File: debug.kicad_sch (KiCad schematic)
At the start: 36 parts, among them J701 USB4105-GF-A, J702 Conn_02x10_Odd_Even, U701 USBLC6-2SC6, U702 FT231XQ, U703 TCA9554PW

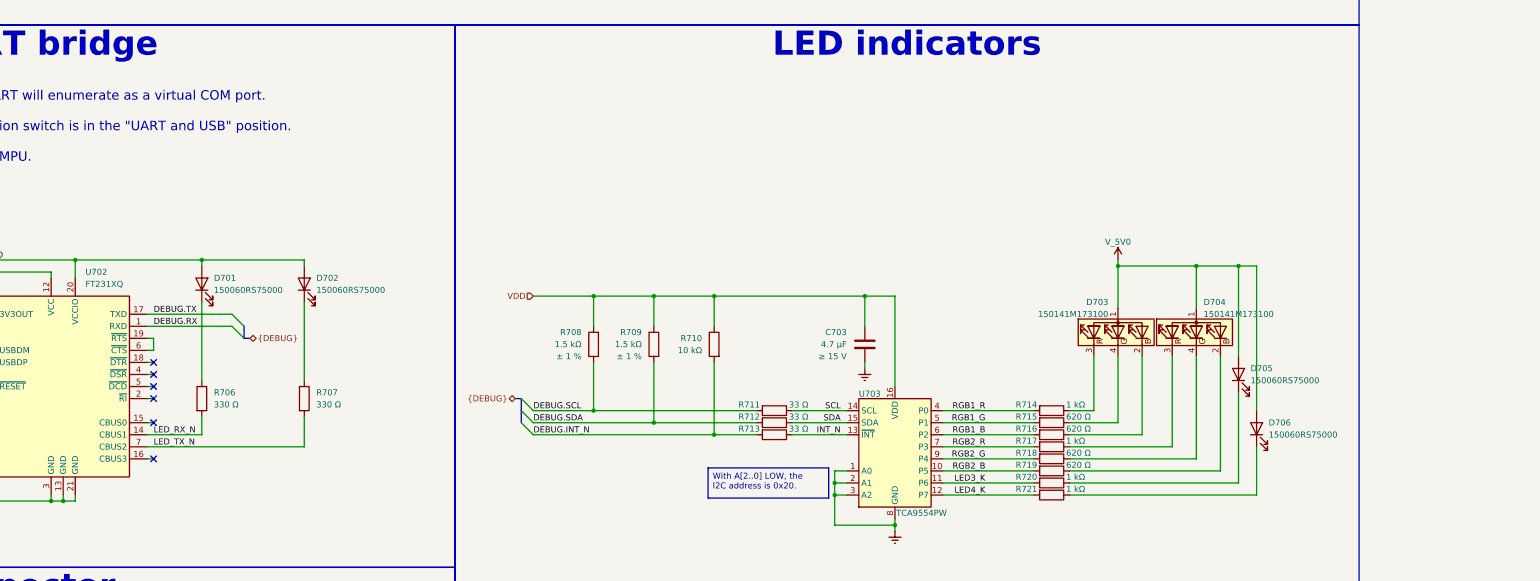
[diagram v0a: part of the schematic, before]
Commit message: Add series termination, assign netclasses, fill schemas' descriptions
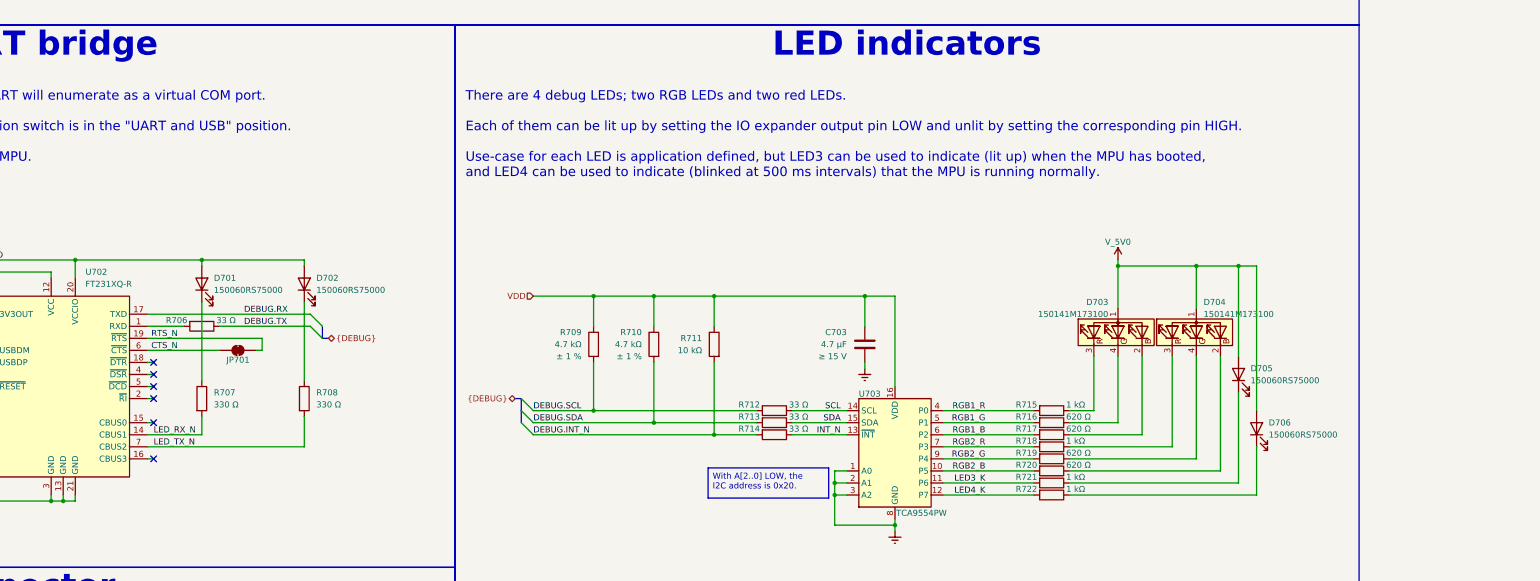
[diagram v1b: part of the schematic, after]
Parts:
- removed R708: 1.5 kΩ, perfect_footprints:R_0402_1005Metric, symbol Device:R
- added JP701: SolderJumper_2_Bridged, Jumper:SolderJumper-2_P1.3mm_Bridged_Pad1.0x1.5mm, symbol Jumper:SolderJumper_2_Bridged
- added R706: 33 Ω, perfect_footprints:R_0402_1005Metric, symbol Device:R
- added R710: 4.7 kΩ, perfect_footprints:R_0402_1005Metric, symbol Device:R
- R709: value 1.5 kΩ -> 4.7 kΩ
- U702: value FT231XQ -> FT231XQ-R; Digi-Key Part Number (none) -> 768-1128-1-ND; MPN (none) -> FT231XQ-R; Manufacturer (none) -> FTDI, Future Technology Devices International Ltd
- renumbered R706 to R707, R707 to R708, R710 to R711, R711 to R712, R712 to R713, R713 to R714, R714 to R715, R715 to R716, R716 to R717, R717 to R718, R718 to R719, R719 to R720, R720 to R721, R721 to R722
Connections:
- net DEBUG.RX: now also U702.17 (TXD); no longer U702.1 (RXD)
- net DEBUG.SCL: now also R709.2
- net DEBUG.SDA: now also R710.2; no longer R709.2
- net DEBUG.TX: now also R706.1; no longer U702.17 (TXD)
- net VDD: now also R710.1
- net CTS_N: now reaches U702.6 (~{CTS})
- net CTS_N: now also JP701.1 (A); no longer U702.19 (~{RTS})
- new net: R706.2, U702.1 (RXD)
- new net RTS_N: JP701.2 (B), U702.19 (~{RTS})

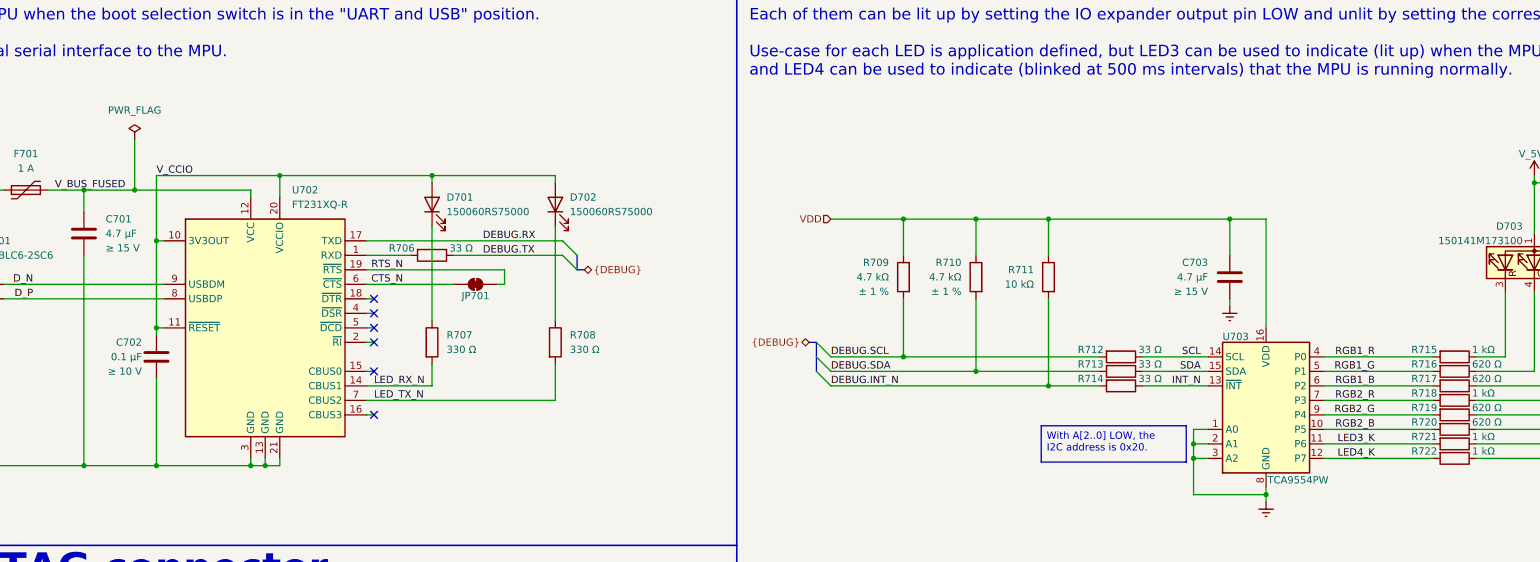
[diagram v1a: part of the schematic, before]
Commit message: Add test points, assign netclasses and clean-up
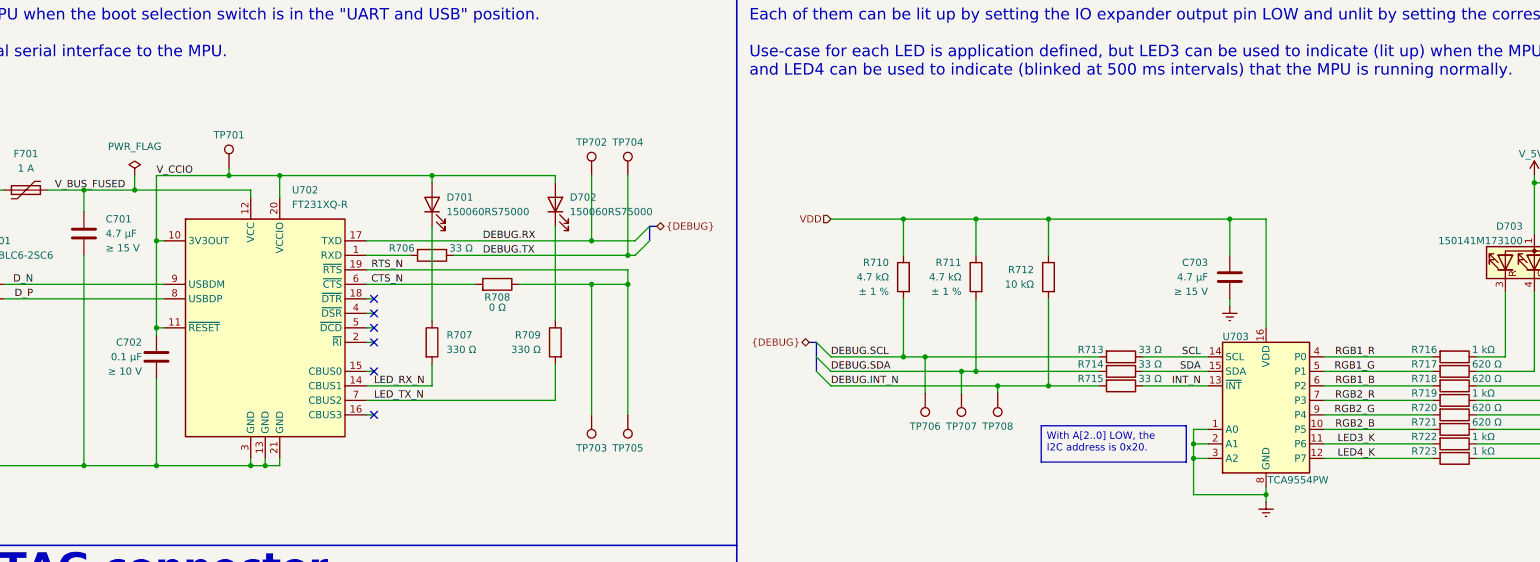
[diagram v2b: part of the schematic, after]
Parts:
- removed JP701: SolderJumper_2_Bridged, Jumper:SolderJumper-2_P1.3mm_Bridged_Pad1.0x1.5mm, symbol Jumper:SolderJumper_2_Bridged
- added R708: 0 Ω, Resistor_SMD:R_0805_2012Metric, symbol Device:R
- added TP701, TP702, TP703, TP704, TP705, TP706, TP707, TP708: TestPoint, TestPoint:TestPoint_Pad_D1.0mm, symbol Connector:TestPoint
- renumbered R708 to R709, R709 to R710, R710 to R711, R711 to R712, R712 to R713, R713 to R714, R714 to R715, R715 to R716, R716 to R717, R717 to R718, R718 to R719, R719 to R720, R720 to R721, R721 to R722, R722 to R723
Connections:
- net CTS_N: now also R708.2
- net DEBUG.INT_N: now also TP708.1
- net DEBUG.RX: now also TP702.1
- net DEBUG.SCL: now also TP706.1
- net DEBUG.SDA: now also TP707.1
- net DEBUG.TX: now also TP704.1
- net RTS_N: now also R708.1, TP703.1, TP705.1
- net V_CCIO: now also TP701.1

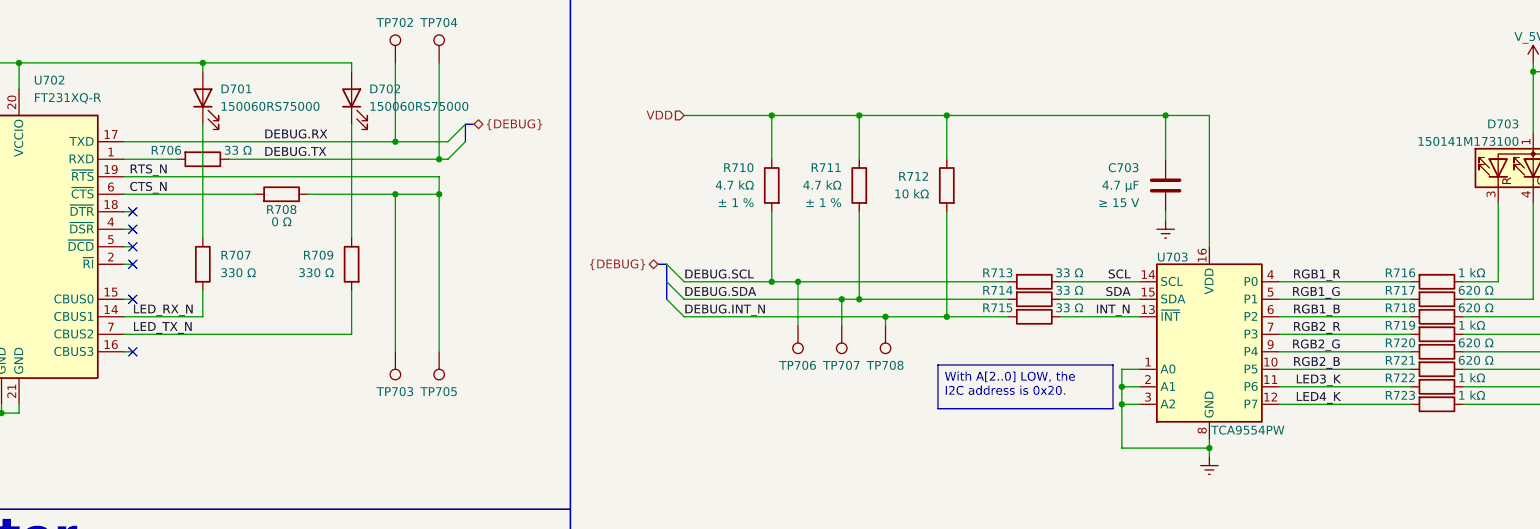
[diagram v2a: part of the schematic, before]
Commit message: Add series termination, refactor schematics
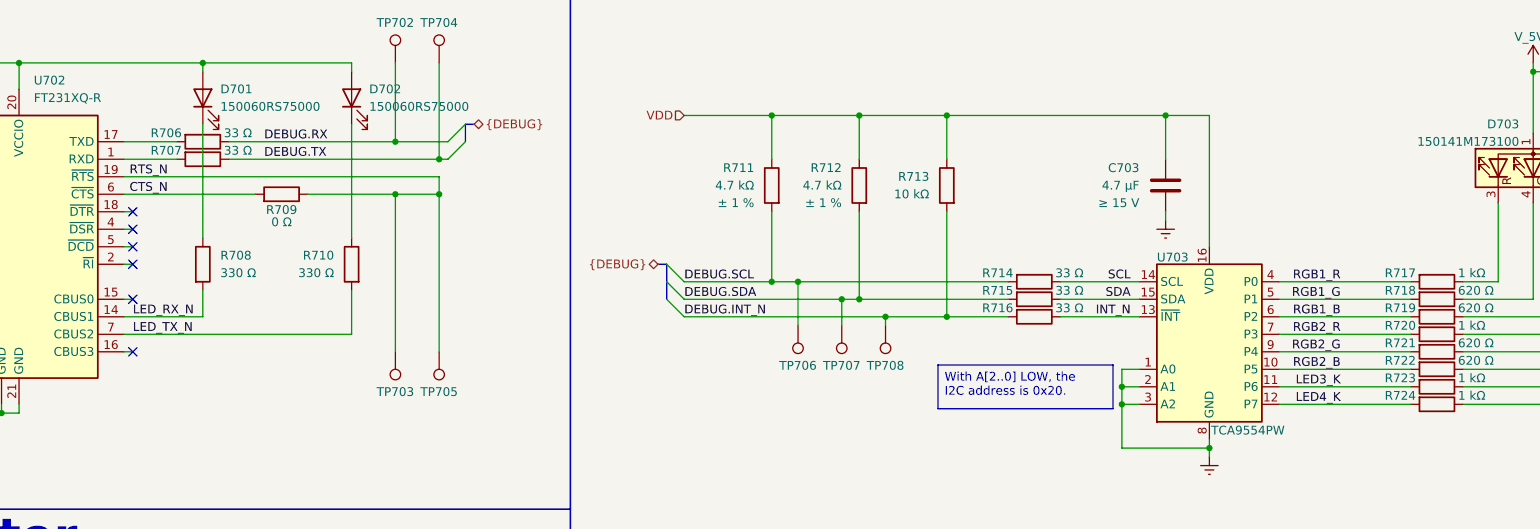
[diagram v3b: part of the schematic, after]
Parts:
- added R706: 33 Ω, perfect_footprints:R_0402_1005Metric, symbol Device:R
- renumbered R706 to R707, R707 to R708, R708 to R709, R709 to R710, R710 to R711, R711 to R712, R712 to R713, R713 to R714, R714 to R715, R715 to R716, R716 to R717, R717 to R718, R718 to R719, R719 to R720, R720 to R721, R721 to R722, R722 to R723, R723 to R724
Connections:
- net DEBUG.RX: now also R706.1; no longer U702.17 (TXD)
- new net: R706.2, U702.17 (TXD)
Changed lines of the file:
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@@
 	(wire
 		(pts
+			(xy 166.37 111.76) (xy 190.5 111.76)
+		)
+		(stroke
+			(width 0)
+			(type default)
+		)
+	)
+	(wire
+		(pts
 			(xy 74.93 200.66) (xy 76.2 200.66)
 		)
@@
 	(wire
 		(pts
-			(xy 151.13 111.76) (xy 190.5 111.76)
+			(xy 151.13 111.76) (xy 158.75 111.76)
 		)
 		(stroke
@@
 		(on_board yes)
 		(dnp no)
-		(property "Reference" "R721"
+		(property "Reference" "R722"
 			(at 338.582 144.272 90)
 			(effects
@@
 			(project "linux-sbc"
 				(path "/fa11a02f-8043-4153-ab69-88d766503017/5e32b227-0684-45b9-8c92-9550e4036164"
-					(reference "R721")
+					(reference "R722")
 					(unit 1)
 				)
@@
 		(on_board yes)
 		(dnp no)
-		(property "Reference" "R715"
+		(property "Reference" "R716"
 			(at 280.162 136.652 90)
 			(effects
@@
 			(project "linux-sbc"
 				(path "/fa11a02f-8043-4153-ab69-88d766503017/5e32b227-0684-45b9-8c92-9550e4036164"
-					(reference "R715")
+					(reference "R716")
 					(unit 1)
 				)
@@
 		(on_board yes)
 		(dnp no)
-		(property "Reference" "R716"
+		(property "Reference" "R717"
 			(at 338.582 131.572 90)
 			(effects
@@
 			(project "linux-sbc"
 				(path "/fa11a02f-8043-4153-ab69-88d766503017/5e32b227-0684-45b9-8c92-9550e4036164"
-					(reference "R716")
+					(reference "R717")
 					(unit 1)
 				)
@@
 		(on_board yes)
 		(dnp no)
-		(property "Reference" "R710"
+		(property "Reference" "R711"
 			(at 242.57 115.57 0)
 			(effects
@@
 			(project "linux-sbc"
 				(path "/fa11a02f-8043-4153-ab69-88d766503017/5e32b227-0684-45b9-8c92-9550e4036164"
-					(reference "R710")
+					(reference "R711")
 					(unit 1)
 				)
@@
 		(on_board yes)
 		(dnp no)
-		(property "Reference" "R720"
+		(property "Reference" "R721"
 			(at 338.582 141.732 90)
 			(effects
@@
 			(project "linux-sbc"
 				(path "/fa11a02f-8043-4153-ab69-88d766503017/5e32b227-0684-45b9-8c92-9550e4036164"
-					(reference "R720")
+					(reference "R721")
 					(unit 1)
 				)
@@
 		(on_board yes)
 		(dnp no)
-		(property "Reference" "R713"
+		(property "Reference" "R714"
 			(at 280.162 131.572 90)
 			(effects
@@
 			(project "linux-sbc"
 				(path "/fa11a02f-8043-4153-ab69-88d766503017/5e32b227-0684-45b9-8c92-9550e4036164"
-					(reference "R713")
+					(reference "R714")
 					(unit 1)
 				)
@@
 		(on_board yes)
 		(dnp no)
-		(property "Reference" "R714"
+		(property "Reference" "R715"
 			(at 280.162 134.112 90)
 			(effects
@@
 			(project "linux-sbc"
 				(path "/fa11a02f-8043-4153-ab69-88d766503017/5e32b227-0684-45b9-8c92-9550e4036164"
-					(reference "R714")
+					(reference "R715")
 					(unit 1)
 				)
@@
 	)
 	(symbol
+		(lib_id "Device:R")
+		(at 162.56 111.76 270)
+		(unit 1)
+		(exclude_from_sim no)
+		(in_bom yes)
+		(on_board yes)
+		(dnp no)
+		(property "Reference" "R706"
+			(at 159.512 111.252 90)
+			(effects
+				(font
+					(size 1.27 1.27)
+				)
+				(justify right bottom)
+			)
+		)
+		(property "Value" "33 Ω"
+			(at 165.608 111.252 90)
+			(effects
+				(font
+					(size 1.27 1.27)
+				)
+				(justify left bottom)
+			)
+		)
+		(property "Footprint" "perfect_footprints:R_0402_1005Metric"
+			(at 162.56 109.982 90)
+			(effects
+				(font
+					(size 1.27 1.27)
+				)
+				(hide yes)
+			)
+		)
+		(property "Datasheet" "https://www.we-online.com/components/products/datasheet/560112110020.pdf"
+			(at 162.56 111.76 0)
+			(effects
+				(font
+					(size 1.27 1.27)
+				)
+				(hide yes)
+			)
+		)
+		(property "Description" "Resistor"
+			(at 162.56 111.76 0)
+			(effects
+				(font
+					(size 1.27 1.27)
+				)
+				(hide yes)
+			)
+		)
+		(property "DigiKey Part Number" "732-560112110020CT-ND"
+			(at 162.56 111.76 0)
+			(effects
+				(font
+					(size 1.27 1.27)
+				)
+				(hide yes)
+			)
+		)
+		(property "MPN" "560112110020"
+			(at 162.56 111.76 0)
+			(effects
+				(font
+					(size 1.27 1.27)
+				)
+				(hide yes)
+			)
+		)
+		(property "Manufacturer" "Würth Elektronik"
+			(at 162.56 111.76 0)
+			(effects
+				(font
+					(size 1.27 1.27)
+				)
+				(hide yes)
+			)
+		)
+		(property "Temperature Coefficient" ""
+			(at 162.56 111.76 0)
+			(effects
+				(font
+					(size 1.27 1.27)
+				)
+				(hide yes)
+			)
+		)
+		(pin "2"
+		)
+		(pin "1"
+		)
+		(instances
+			(project "linux-sbc"
+				(path "/fa11a02f-8043-4153-ab69-88d766503017/5e32b227-0684-45b9-8c92-9550e4036164"
+					(reference "R706")
+					(unit 1)
+				)
+			)
+		)
+	)
+	(symbol
 		(lib_id "Device:LED_ABRG")
 		(at 355.6 115.57 90)
@@
 		(on_board yes)
 		(dnp no)
-		(property "Reference" "R717"
+		(property "Reference" "R718"
 			(at 338.582 134.112 90)
 			(effects
@@
 			(project "linux-sbc"
 				(path "/fa11a02f-8043-4153-ab69-88d766503017/5e32b227-0684-45b9-8c92-9550e4036164"
-					(reference "R717")
+					(reference "R718")
 					(unit 1)
 				)
@@
 		(on_board yes)
 		(dnp no)
-		(property "Reference" "R711"
+		(property "Reference" "R712"
 			(at 255.27 115.57 0)
 			(effects
@@
 			(project "linux-sbc"
 				(path "/fa11a02f-8043-4153-ab69-88d766503017/5e32b227-0684-45b9-8c92-9550e4036164"
-					(reference "R711")
+					(reference "R712")
 					(unit 1)
 				)
@@
 		(on_board yes)
 		(dnp no)
-		(property "Reference" "R709"
+		(property "Reference" "R710"
 			(at 181.61 128.2699 0)
 			(effects
@@
 			(project "linux-sbc"
 				(path "/fa11a02f-8043-4153-ab69-88d766503017/5e32b227-0684-45b9-8c92-9550e4036164"
-					(reference "R709")
+					(reference "R710")
 					(unit 1)
 				)
@@
 		(on_board yes)
 		(dnp no)
-		(property "Reference" "R719"
+		(property "Reference" "R720"
 			(at 338.582 139.192 90)
 			(effects
@@
 			(project "linux-sbc"
 				(path "/fa11a02f-8043-4153-ab69-88d766503017/5e32b227-0684-45b9-8c92-9550e4036164"
-					(reference "R719")
+					(reference "R720")
 					(unit 1)
 				)
@@
 		(on_board yes)
 		(dnp no)
-		(property "Reference" "R722"
+		(property "Reference" "R723"
 			(at 338.582 146.812 90)
 			(effects
@@
 			(project "linux-sbc"
 				(path "/fa11a02f-8043-4153-ab69-88d766503017/5e32b227-0684-45b9-8c92-9550e4036164"
-					(reference "R722")
+					(reference "R723")
 					(unit 1)
 				)
@@
 		(on_board yes)
 		(dnp no)
-		(property "Reference" "R718"
+		(property "Reference" "R719"
 			(at 338.582 136.652 90)
 			(effects
@@
 			(project "linux-sbc"
 				(path "/fa11a02f-8043-4153-ab69-88d766503017/5e32b227-0684-45b9-8c92-9550e4036164"
-					(reference "R718")
+					(reference "R719")
 					(unit 1)
 				)
@@
 		(on_board yes)
 		(dnp no)
-		(property "Reference" "R708"
+		(property "Reference" "R709"
 			(at 173.99 120.904 90)
 			(effects
@@
 			(project "linux-sbc"
 				(path "/fa11a02f-8043-4153-ab69-88d766503017/5e32b227-0684-45b9-8c92-9550e4036164"
-					(reference "R708")
+					(reference "R709")
 					(unit 1)
 				)
@@
 		(on_board yes)
 		(dnp no)
-		(property "Reference" "R723"
+		(property "Reference" "R724"
 			(at 338.582 149.352 90)
 			(effects
@@
 			(project "linux-sbc"
 				(path "/fa11a02f-8043-4153-ab69-88d766503017/5e32b227-0684-45b9-8c92-9550e4036164"
-					(reference "R723")
+					(reference "R724")
 					(unit 1)
 				)
@@
 		(on_board yes)
 		(dnp no)
-		(property "Reference" "R707"
+		(property "Reference" "R708"
 			(at 165.1 128.2699 0)
 			(effects
@@
 			(project "linux-sbc"
 				(path "/fa11a02f-8043-4153-ab69-88d766503017/5e32b227-0684-45b9-8c92-9550e4036164"
-					(reference "R707")
+					(reference "R708")
 					(unit 1)
 				)
@@
 		(on_board yes)
 		(dnp no)
-		(property "Reference" "R712"
+		(property "Reference" "R713"
 			(at 267.97 116.8399 0)
 			(effects
@@
 			(project "linux-sbc"
 				(path "/fa11a02f-8043-4153-ab69-88d766503017/5e32b227-0684-45b9-8c92-9550e4036164"
-					(reference "R712")
+					(reference "R713")
 					(unit 1)
 				)
@@
 		(on_board yes)
 		(dnp no)
-		(property "Reference" "R706"
+		(property "Reference" "R707"
 			(at 159.512 113.792 90)
 			(effects
@@
 			(project "linux-sbc"
 				(path "/fa11a02f-8043-4153-ab69-88d766503017/5e32b227-0684-45b9-8c92-9550e4036164"
-					(reference "R706")
+					(reference "R707")
 					(unit 1)
 				)

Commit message: Refactor symbol properties
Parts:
- C701, C703: DigiKey Part Number 490-7205-1-ND -> (none)
- D701, D702, D705, D706: DigiKey Part Number 732-4978-1-ND -> (none)
- R701, R703, R704, R706, R707, R713, R714, R715, R716, R717, R718, R719, R720, R721, R722, R723, R724: DigiKey Part Number 732-560112110020CT-ND -> (none)
- R708, R710: DigiKey Part Number 732-560112110019CT-ND -> (none)
- R709: DigiKey Part Number 732-560112120002CT-ND -> (none)

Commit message: Refactor debug
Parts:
- renumbered R703 to R702, R702 to R703, R708 to R706, R710 to R707, R706 to R708, R707 to R709, R709 to R710
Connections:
- net CTS_N: now also TP702.1
- net DEBUG.RX: now also TP704.1; no longer TP702.1
- net DEBUG.TX: now also TP705.1; no longer TP704.1
- net RTS_N: no longer TP705.1
- net TXD: now reaches R708.2, U702.17 (TXD)
- net RXD: now reaches R709.2, U702.1 (RXD)
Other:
- moved on the sheet: C701, C702, C703, D701, D702, D703, D704, D705, D706, F701, J701, J702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
